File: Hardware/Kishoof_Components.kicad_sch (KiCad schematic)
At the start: 113 parts, among them J1 SWD_Header, J10 VOct, J11 WavetablePosA, J12 WavetablePos, J13 VCA, J14 Conn_01x02_Socket, J15 Conn_01x02_Socket, J16 Conn_01x02_Socket, J17 Conn_01x02_Socket, J18 USB_C_Receptacle, J2 Eurorack_10_pin_power, J4 Conn_01x01_Socket, J7 Audio_Out_L, J8 Audio_Out_R, J9 WarpCV, SW1 Encoder, SW2 Mode_Switch, SW3 Octave_Switch, SW4 ChB_Output, SW5 SW_Push, U1 STM32H7B0VBTx, U2 PCM5100APW, U3 TPS561201, U4 LT1117-3.3, U5 MCP6002, U6 MX25LM51245G, U7 MCP6004, U8 TL072, U9 STF202-22T1G, Y1 8MHz 20pF

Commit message: Added LCD Riser board; power routing
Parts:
- removed J14, J15, J16, J17: Conn_01x02_Socket, Connector_PinSocket_2.54mm:PinSocket_1x02_P2.54mm_Vertical, symbol Connector:Conn_01x02_Socket
- added U10: ~, Custom_Footprints:LCD_Riser, symbol Mountjoy:LCD_Riser
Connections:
- net +3.3V: now also U10.7 (VDD)
- net ENCODER_BTN: now also U1.88 (PD7); no longer U1.65 (PC8)
- net GND: now also U1.32 (PC4), U10.6 (GND)
- net LCD_BACKLIGHT: now also U10.8 (BACKLIGHT)
- net LCD_DC: now also U10.3 (DC)
- net LCD_RESET: now also U10.4 (RESET)
- net LCD_SPI3_MOSI: now also U10.1 (MOSI)
- net LCD_SPI3_SCK: now also U10.2 (CLK)
- net LCD_SPI3_SS: now also U10.5 (CS)
- net VcaCV: now also U1.30 (PA6); no longer U1.31 (PA7)
- net WAVETABLE_POS_A_POT: now also U1.31 (PA7); no longer U1.30 (PA6)
- no-connect marks 47 -> 46
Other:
- note added: "Grounded for A/D signal separation"

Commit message: Added STM32H7B0 project for testing
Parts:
- removed TP1: TestPoint, TestPoint:TestPoint_Pad_D1.0mm, symbol Connector:TestPoint
- added D4: LED_Small, LED_THT:LED_D3.0mm_FlatTop, symbol Device:LED_Small
- added J3: Conn_01x02_Pin, Connector_PinHeader_2.54mm:PinHeader_1x02_P2.54mm_Vertical, symbol Connector:Conn_01x02_Pin
- added R30: 1k, Resistor_SMD:R_0603_1608Metric, symbol Device:R_Small
- added R31: 100k, Resistor_SMD:R_0603_1608Metric, symbol Device:R_Small
- added TP2, TP3, TP4, TP5, TP6, TP7, TP8: TestPoint, Connector_PinSocket_2.54mm:PinSocket_1x01_P2.54mm_Vertical, symbol Connector:TestPoint
- J4: footprint Connector_PinSocket_2.54mm:PinSocket_1x01_P2.54mm_Vertical -> Connector_PinHeader_2.54mm:PinHeader_1x01_P2.54mm_Vertical
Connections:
- net +12V: now also TP2.1
- net +3.3V: now also TP5.1
- net +3.3VA: now also TP6.1
- net -12V: now also TP3.1
- net -5V_REF: now also TP7.1
- net EXT_AUDIO_IN: now also R31.1
- net GND: now also D4.1 (K), R31.2, TP4.1, TP8.1
- net LED_B_Oct: now reaches U1.61 (PD14)
- net LED_B_Oct: now also R30.1
- net UART_TX: now reaches U1.86 (PD5)
- net UART_TX: now also J3.1 (Pin_1)
- net UART_RX: now reaches U1.87 (PD6)
- net UART_RX: now also J3.2 (Pin_2)
- net B_Octave_Btn1 renamed B_Octave_Btn
- net RESET: no longer names the net of U1.14 (NRST)
- new net LED_OCT_B: D4.2 (A), R30.2
- no-connect marks 46 -> 44

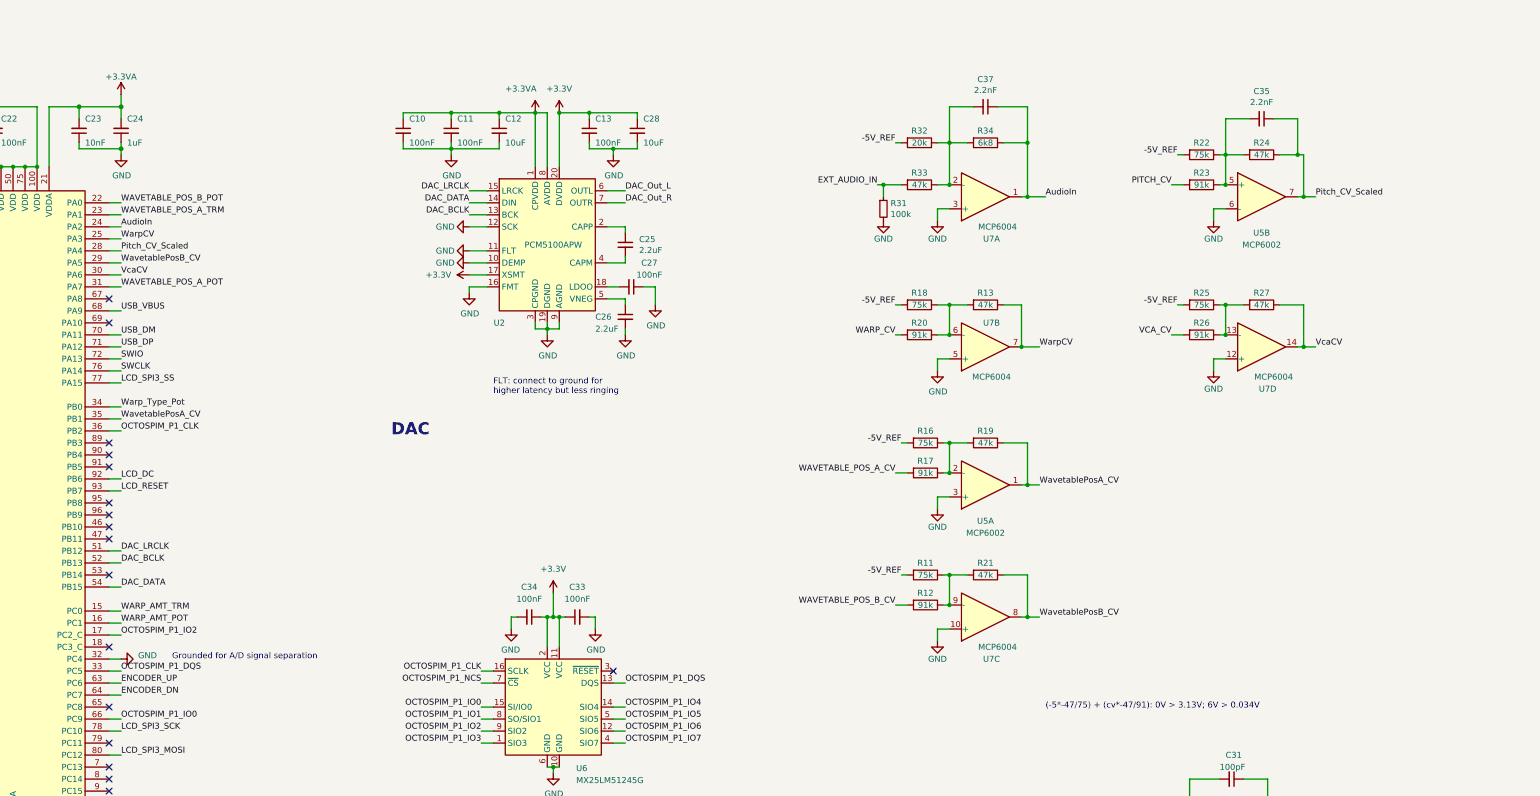
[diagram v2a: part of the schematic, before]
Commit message: Updating JLC assembly part number
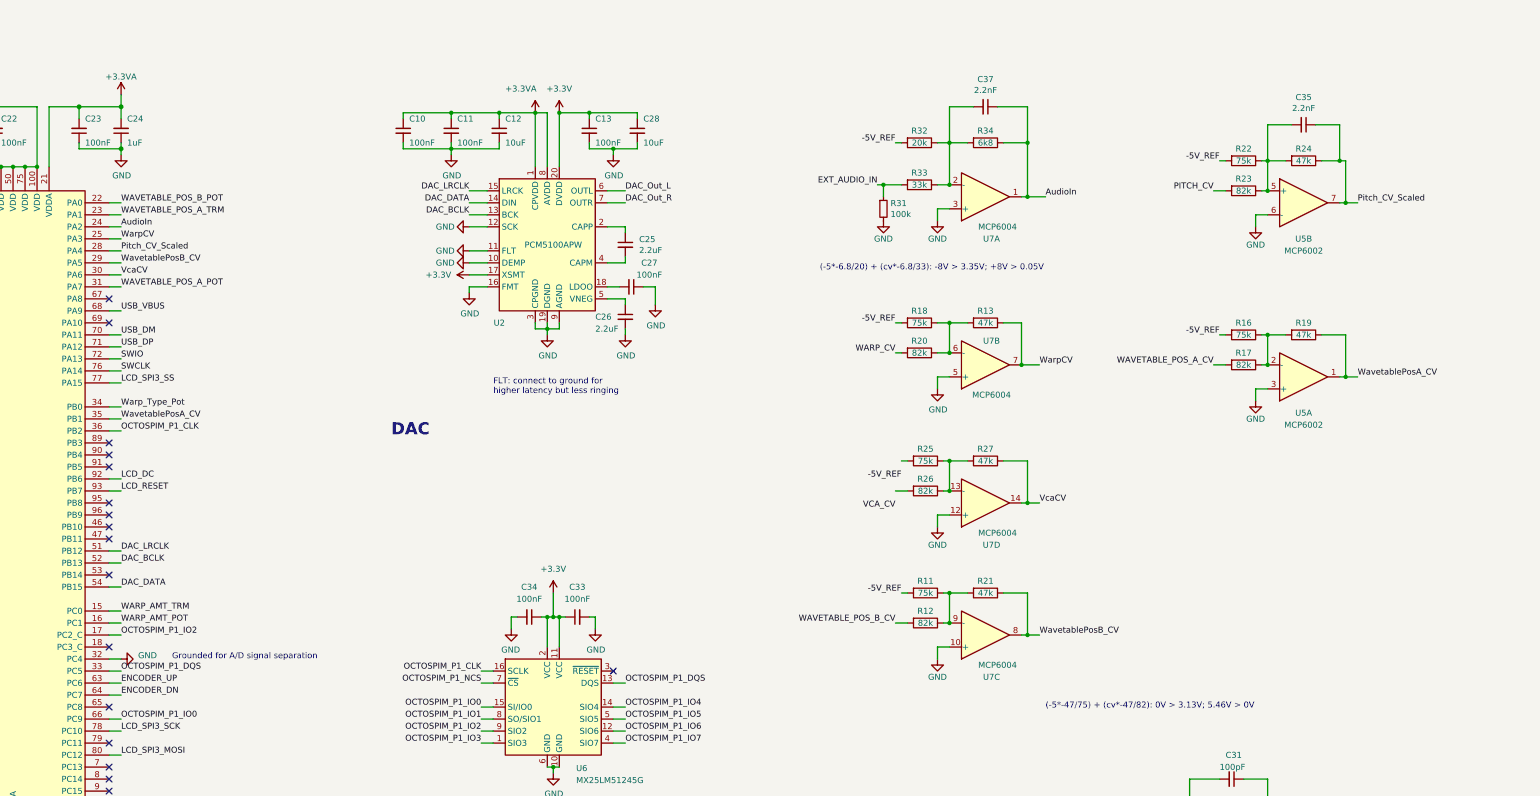
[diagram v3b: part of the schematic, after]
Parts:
- C23: value 10nF -> 100nF
- C29, C30: Part_Number C1588 -> C1604
- C35, C37: Part_Number C1595 -> C1604
- C38, C39: Part_Number C15849 -> C23630
- C8: Part_Number C57112 -> C14663
- D1, D2: Part_Number (none) -> C8598
- L2: Part_Number C326343 -> (none)
- R1: Part_Number (none) -> C25819
- R10, R30, R9: Part_Number (none) -> C4190
- R12, R17, R20, R23, R26: value 91k -> 82k
- R13: Part_Number C23206 -> C25819
- R15: Part_Number (none) -> C23345
- R2: Part_Number (none) -> C25804
- R28, R29: Part_Number (none) -> C23186
- R31: Part_Number (none) -> C25803
- R33: value 47k -> 33k
- U2: Part_Number C131154 -> (none)
- U7: Part_Number C116668 -> (none)
- U8: Part_Number (none) -> C6961
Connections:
- net -5V_REF: no longer R25.2
- net VCA_CV: no longer R26.2
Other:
- note added: "(-5*-47/75) + (cv*-47/82): 0V > 3.13V; 5.46V > 0V"
- note added: "(-5*-6.8/20) + (cv*-6.8/33): -8V > 3.35V; +8V > 0.05V"
- note removed: "(-5*-47/75) + (cv*-47/91): 0V > 3.13V; 6V > 0.034V"
- moved on the sheet: C35, R11, R12, R13, R16, R17, R18, R19, R20, R21, R22, R23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

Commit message: Schematic Clean up
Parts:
- removed D4: LED_Small, LED_THT:LED_D3.0mm_FlatTop, symbol Device:LED_Small
- removed J10: VOct, Custom_Footprints:THONKICONN_hole, symbol thonkiconn:AudioJack2_Ground_Switch
- removed J11: WavetablePosA, Custom_Footprints:THONKICONN_hole, symbol thonkiconn:AudioJack2_Ground_Switch
- removed J12: WavetablePos, Custom_Footprints:THONKICONN_hole, symbol thonkiconn:AudioJack2_Ground_Switch
- removed J13: VCA, Custom_Footprints:THONKICONN_hole, symbol thonkiconn:AudioJack2_Ground_Switch
- removed J18: USB_C_Receptacle, Custom_Footprints:USB_C_Receptacle_Amphenol_12401951E412A, symbol Connector:USB_C_Receptacle
- removed J3: Conn_01x02_Pin, Connector_PinHeader_2.54mm:PinHeader_1x02_P2.54mm_Vertical, symbol Connector:Conn_01x02_Pin
- removed J4: Conn_01x01_Socket, Connector_PinHeader_2.54mm:PinHeader_1x01_P2.54mm_Vertical, symbol Connector:Conn_01x01_Socket
- removed J7: Audio_Out_L, Custom_Footprints:THONKICONN_hole, symbol thonkiconn:AudioJack2_Ground_Switch
- removed J8: Audio_Out_R, Custom_Footprints:THONKICONN_hole, symbol thonkiconn:AudioJack2_Ground_Switch
- removed J9: WarpCV, Custom_Footprints:THONKICONN_hole, symbol thonkiconn:AudioJack2_Ground_Switch
- removed R28, R29: 5k1, Resistor_SMD:R_0603_1608Metric, symbol Device:R_Small
- removed SW1: Encoder, Custom_Footprints:Encoder, symbol Device:RotaryEncoder_Switch
- removed SW2: Mode_Switch, Custom_Footprints:SPDT_Miniature, symbol Switch:SW_SPDT
- removed SW3: Octave_Switch, Custom_Footprints:SP3T_Mini_Switch, symbol Switch:SW_SPDT_MSM
- removed SW4: ChB_Output, Custom_Footprints:SP3T_Mini_Switch, symbol Switch:SW_SPDT_MSM
- removed SW5: SW_Push, Custom_Footprints:SW_PUSH_6mm_aligned, symbol Switch:SW_Push
- removed U10: ~, Custom_Footprints:LCD_Riser, symbol Mountjoy:LCD_Riser
- removed WarpAmtPot1, WarpAmtTrm2, WavetableAPot1, WavetableATrm1, WavetableBPot1: B10k, Custom_Footprints:Alpha_9mm_Potentiometer_Aligned, symbol Device:R_Potentiometer
- removed WarpType1: WarpTypePot, Custom_Footprints:Bourns_Switch_Potentiometer, symbol Mountjoy:Switch_Potentiometer
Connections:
- net -5V_REF: now also R25.2
- net VCA_CV_In: now reaches R26.2
- net AUDIO_OUT_L renamed Audio_Out_L
- net AUDIO_OUT_R renamed Audio_Out_R
- net ENCODER_BTN renamed Encoder_Btn
- net ENCODER_DN renamed Encoder_Down
- net ENCODER_UP renamed Encoder_Up
- net EXT_AUDIO_IN renamed Ext_Audio_In
- net LCD_BACKLIGHT renamed LCD_Backlight
- net LED_B_Oct renamed LED_Oct_B
- net LED_OCT_B renamed LED_Oct_B_Out
- net PITCH_CV renamed Pitch_CV_In
- net WARP_AMT_POT renamed Warp_Amt_Pot
- net WARP_AMT_TRM renamed Warp_Amt_Trm
- net WARP_CV renamed Warp_CV_In
- net WAVETABLE_POS_A_CV renamed Wavetable_Pos_A_CV_In
- net WAVETABLE_POS_A_POT renamed Wavetable_Pos_A_Pot
- net WAVETABLE_POS_A_TRM renamed Wavetable_Pos_A_Trm
- net WAVETABLE_POS_B_CV renamed Wavetable_Pos_B_CV_In
- net WAVETABLE_POS_B_POT renamed Wavetable_Pos_B_Pot
- no-connect marks 44 -> 32
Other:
- added sheet Kishoof_Controls (Kishoof_Controls.kicad_sch)
- note added: "Input Scaling"
- note added: "Microcontroller"
- note added: "OctoSPI Flash"
- note added: "Power"
- note added: "Protection and Output"
- title: Kishoof -> Kishoof Components
- moved on the sheet: C1, C2, C29, C30, C31, C32, C33, C34, C35, C36, C37, C5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
